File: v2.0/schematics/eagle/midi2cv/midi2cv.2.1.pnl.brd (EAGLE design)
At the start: 100 x 41.9 mm, 22 parts, among them IC1 TL084P, IC3 TL084P, J1 GATE1 OUT, J2 GATE2 OUT, J3 GATE3 OUT, J4 GATE4 OUT, J5 GATE5 OUT, J6 CV3 OUT, J7 CV2 OUT, J8 CV1 OUT

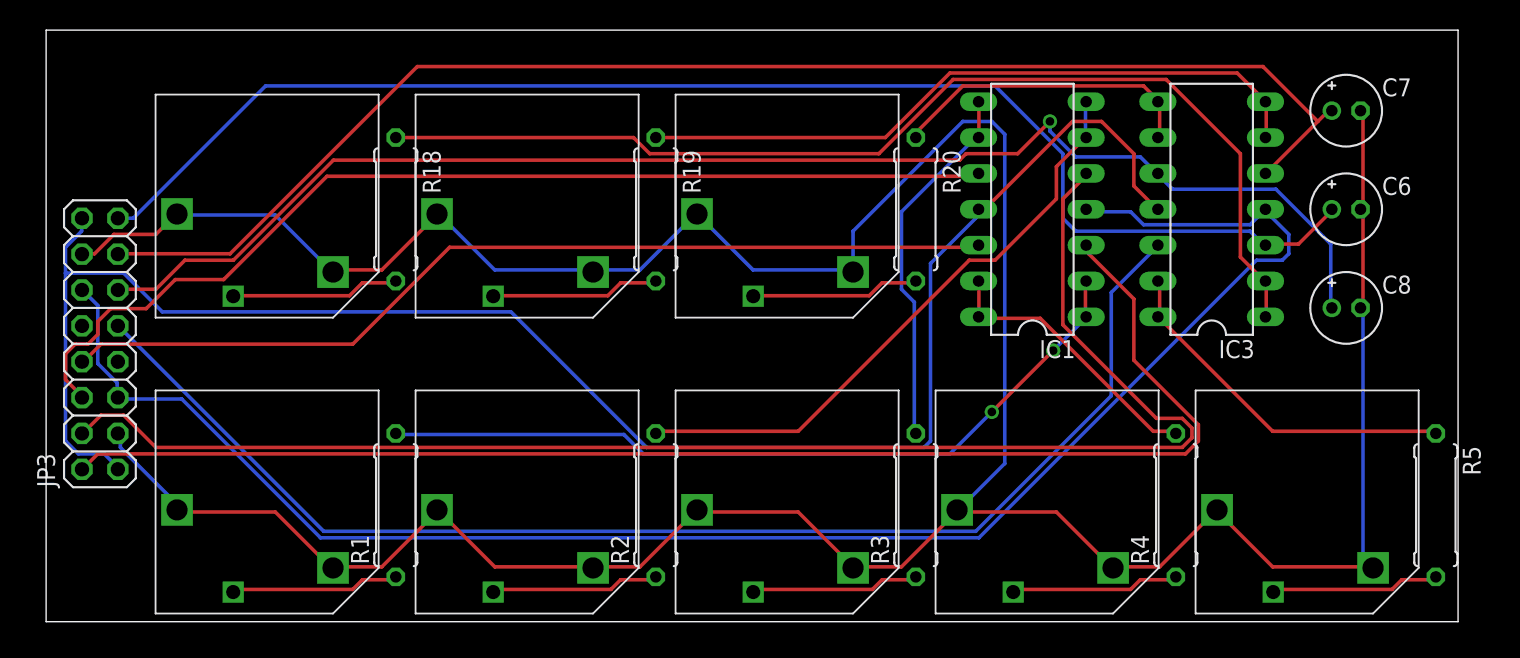
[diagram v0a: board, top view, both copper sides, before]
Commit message: Gerbers generated for midi2cv seeed submission (main and pnl)
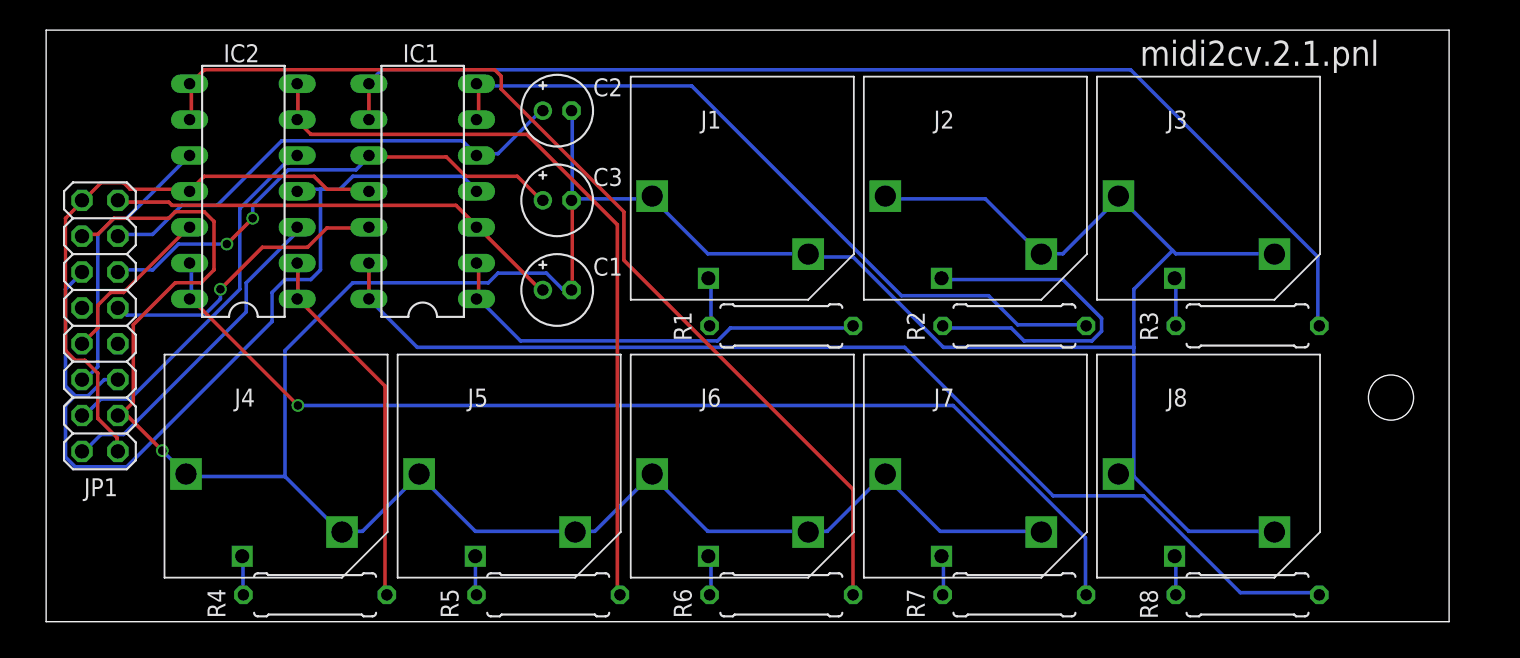
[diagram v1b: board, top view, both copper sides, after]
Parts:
- removed C6, C7, C8: 4.7uF, _common:E2-5
- removed IC3: TL084P, _common:DIL14
- removed JP3: TO BRD, pinhead:2X08
- removed R18, R19, R20: 1K, _common:0309/10
- added C1, C2, C3: 4.7uF, _common:E2-5
- added IC2: TL084P, _common:DIL14
- added JP1: TO MAIN, pinhead:2X08
- added R6, R7, R8: 1K, _common:0309/10
- J1: value GATE1 OUT -> CV3 OUT
- J2: value GATE2 OUT -> CV2 OUT
- J3: value GATE3 OUT -> CV1 OUT
- J4: value GATE4 OUT -> GATE1 OUT
- J5: value GATE5 OUT -> GATE2 OUT
- J6: value CV3 OUT -> GATE3 OUT
- J7: value CV2 OUT -> GATE4 OUT
- J8: value CV1 OUT -> GATE5 OUT
- moved R5 63.2 mm to (35.6, 1.91), turned to 0 degrees
- moved R4 61.3 mm to (19.1, 1.91), turned to 0 degrees
- moved J5 56.6 mm to (37.5, 6.35)
- moved J4 54.7 mm to (21.0, 6.35)
- moved IC1 43.2 mm to (26.7, 30.5)
- moved J1 40.3 mm to (54.0, 26.0)
- moved J2 38.8 mm to (70.5, 26.0)
- moved J6 38.4 mm to (54.0, 6.35)
- moved J3 37.2 mm to (87.0, 26.0)
- moved J7 36.7 mm to (70.5, 6.35)
- moved J8 35.1 mm to (87.0, 6.35)
- moved R1 30.1 mm to (52.1, 21.0), turned to 180 degrees
- moved R2 28.4 mm to (68.6, 21.0), turned to 180 degrees
- moved R3 26.7 mm to (85.1, 21.0), turned to 180 degrees
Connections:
- removed net N$21 (its old number): J1.P$2, R1.1
- new net N$24: J7.P$2, R7.1
- net +12V: now also IC2.4, JP1.12, JP1.5; no longer IC3.4, JP3.12, JP3.5
- net -12V: now also IC2.11, JP1.1, JP1.16; no longer IC3.11, JP3.1, JP3.16
- net 0V: now also C1.-, C2.-, C3.-, JP1.14, JP1.3; no longer C6.-, C7.-, C8.-, JP3.14, JP3.3
- net CV1: now also C3.+, IC1.10, JP1.11; no longer C8.+, IC3.10, JP3.11
- net CV2: now also C2.+, IC1.5, JP1.13; no longer C7.+, IC3.5, JP3.13
- net CV3: now also C1.+, IC1.3, JP1.15; no longer C6.+, IC3.3, JP3.15
- net GATE1: now also IC2.3, JP1.2; no longer IC1.3, JP3.2
- net GATE2: now also IC2.5, JP1.4; no longer IC1.5, JP3.4
- net GATE3: now also IC2.10, JP1.6; no longer IC1.10, JP3.6
- net GATE4: now also IC2.12, JP1.8; no longer IC1.12, JP3.8
- net GATE5: now also IC1.12, JP1.9; no longer IC3.12, JP3.9
- net N$2: now also IC1.1, IC1.2, R1.1; no longer IC3.1, IC3.2, R18.1
- net N$22: now also J5.P$2, R5.1; no longer J2.P$2, R2.1
- net N$23: now also J6.P$2, R6.1; no longer J3.P$2, R3.1
- net N$25: now also J8.P$2, R8.2; no longer J5.P$2, R5.2
- net N$3: now also IC1.6, IC1.7, R2.1; no longer IC3.6, IC3.7, R19.1
- net N$31: now also IC2.13, IC2.14, R7.2; no longer IC1.13, IC1.14, R4.2
- net N$35: now also IC2.8, IC2.9, R6.2; no longer IC1.8, IC1.9, R3.2
- net N$36: now also IC2.6, IC2.7, R5.2; no longer IC1.6, IC1.7, R2.2
- net N$37: now also IC2.1, IC2.2, R4.2; no longer IC1.1, IC1.2, R1.2
- net N$4: now also IC1.8, IC1.9, R3.1; no longer IC3.8, IC3.9, R20.1
- net N$44: now also J1.P$2, R1.2; no longer J6.P$2, R18.2
- net N$45: now also J2.P$2, R2.2; no longer J7.P$2, R19.2
- net N$46: now also J3.P$2, R3.2; no longer J8.P$2, R20.2
- net N$7: now also IC1.13, IC1.14, R8.1; no longer IC3.13, IC3.14, R5.1
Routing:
- net -12V: track 124.5 -> 42.3 mm
- net GATE2: track 104.6 -> 26.2 mm
- net GATE1: track 97.1 -> 23.3 mm
- net GATE5: track 92.4 -> 21.0 mm, vias 0 -> 1
- net CV3: track 98.3 -> 32.7 mm
- net CV2: track 98.8 -> 34.6 mm
- net CV1: track 99.4 -> 35.5 mm, vias 1 -> 2
- net +12V: track 121.5 -> 62.3 mm
- net N$4: track 22.2 -> 80.6 mm
- net N$31: track 20.1 -> 77.3 mm, vias 0 -> 1
- net GATE4: track 66.9 -> 12.0 mm
- net GATE3: track 74.1 -> 19.7 mm
- net N$7: track 25.8 -> 78.5 mm
- net N$35: track 26.3 -> 72.4 mm
- net N$2: track 77.0 -> 31.3 mm
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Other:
- board size 100 x 41.9 mm -> 99.4 x 41.9 mm
- board text added: "midi2cv.2.1.pnl"
